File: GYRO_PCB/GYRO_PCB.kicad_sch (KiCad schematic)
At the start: 17 parts, among them J1 Pmod GYRO, J2 FLASH Socket 1, J3 FLASH Socket 2, J4 Power Terminal, J5 Battery Switch, U1 NUCLEO64-F446RE

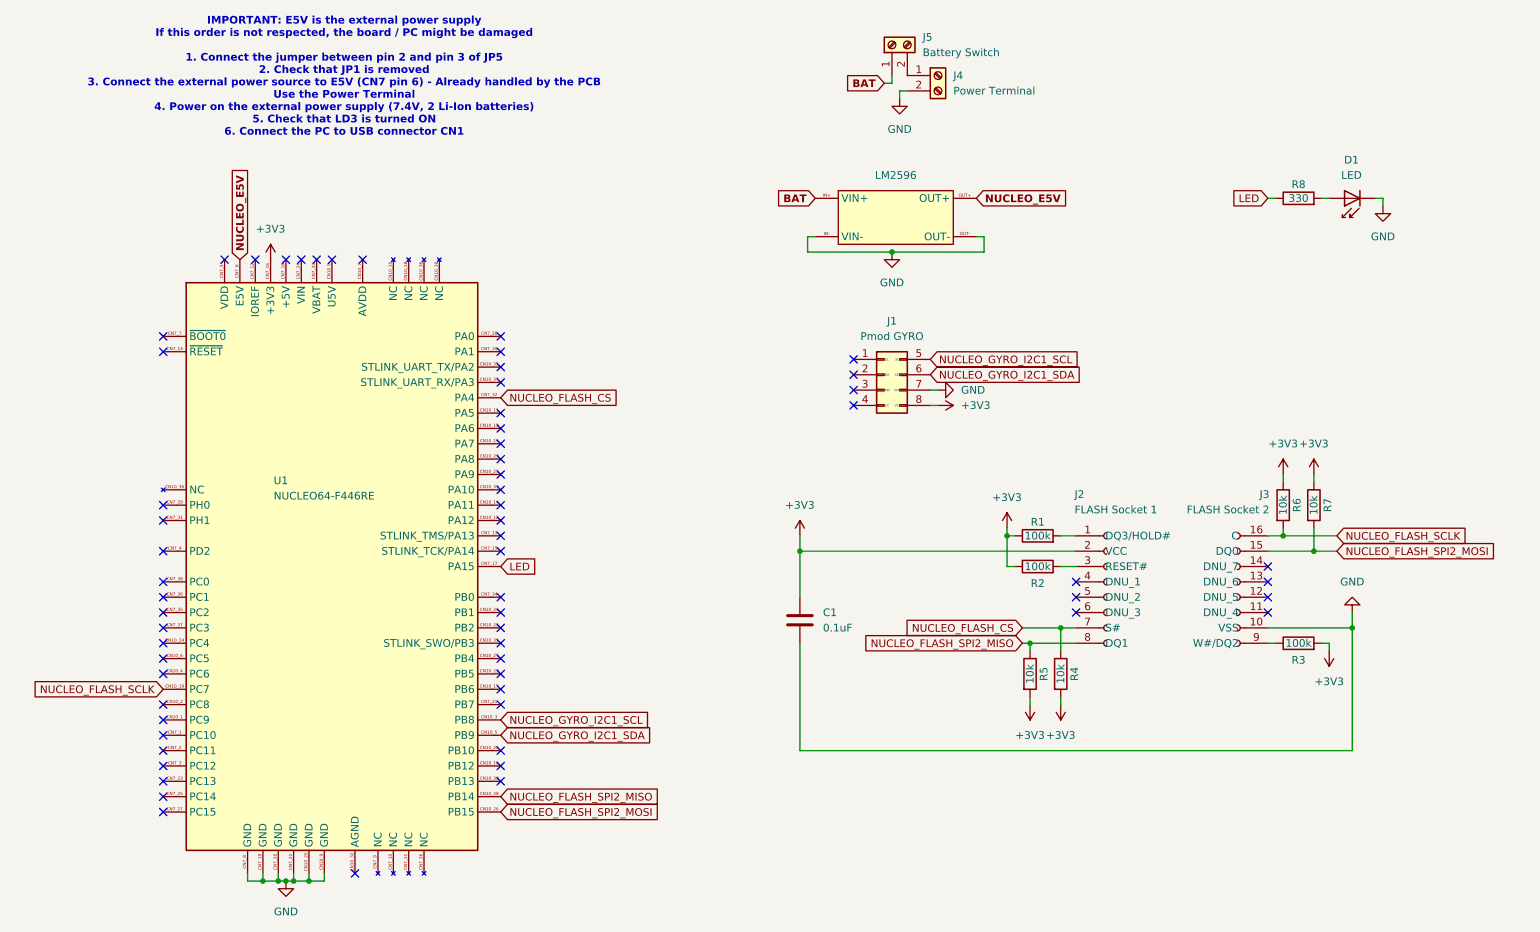
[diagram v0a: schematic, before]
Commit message: feat: add push button
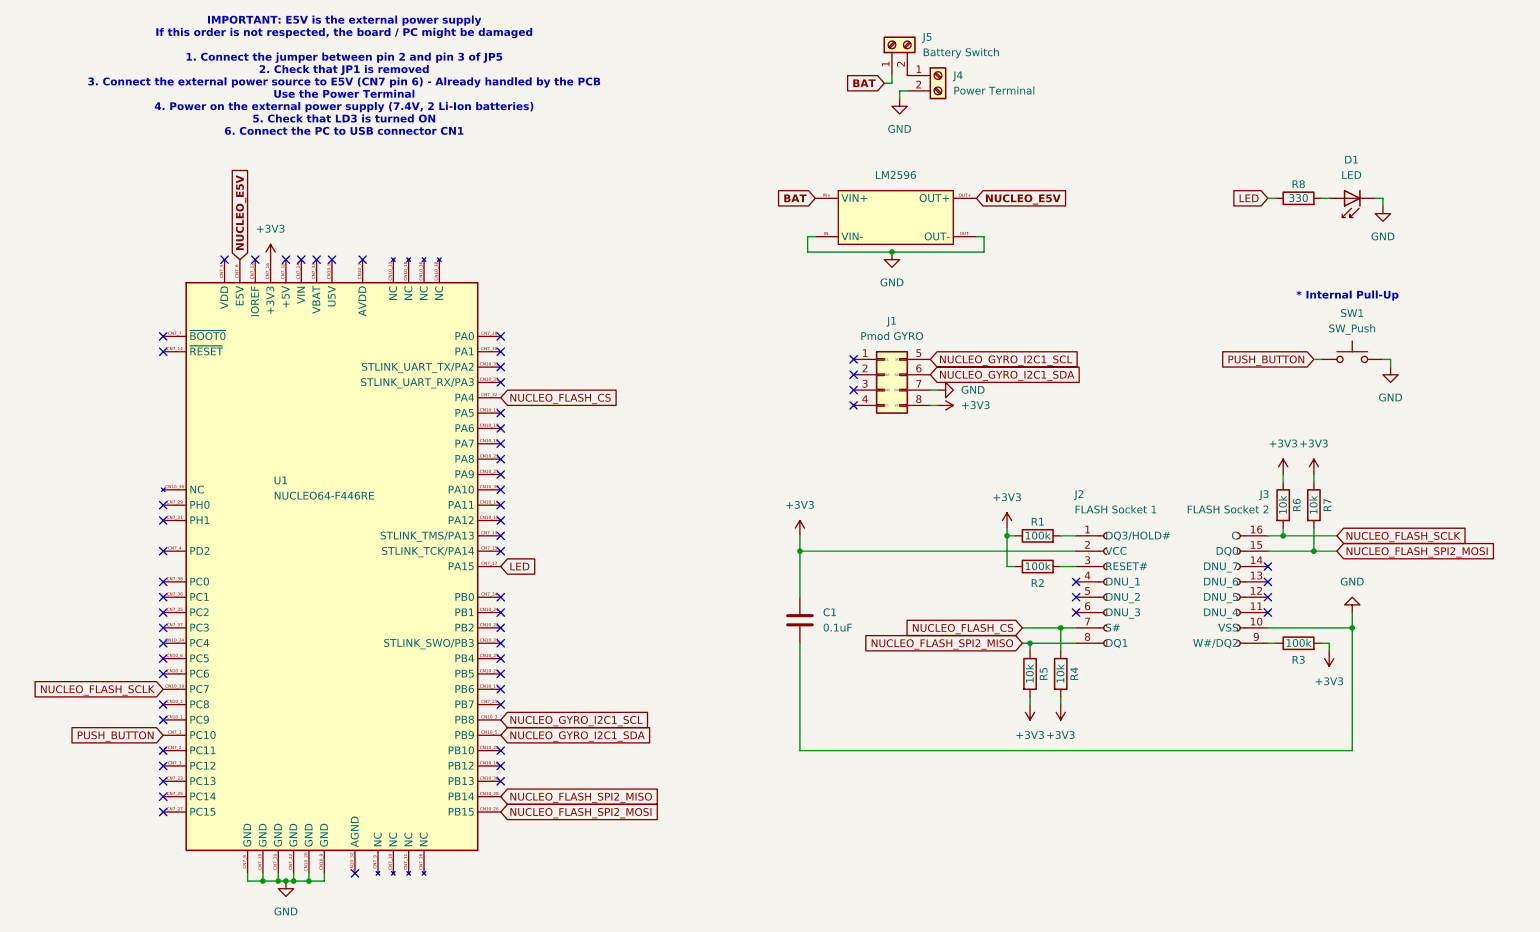
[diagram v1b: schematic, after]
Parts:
- added SW1: SW_Push, Connector_PinSocket_2.54mm:PinSocket_1x02_P2.54mm_Vertical, symbol Switch:SW_Push
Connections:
- net GND: now also SW1.2
- net PUSH_BUTTON: now reaches U1.CN7_1 (PC10)
- net PUSH_BUTTON: now also SW1.1
- no-connect marks 64 -> 63
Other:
- note added: "* Internal Pull-Up"
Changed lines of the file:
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@@
 				(thickness 0.254)
 				(bold yes)
+				(color 255 0 0 1)
+			)
+		)
+	)
+	(text "* Internal Pull-Up"
+		(exclude_from_sim no)
+		(at 248.158 74.676 0)
+		(effects
+			(font
+				(size 1.27 1.27)
+				(thickness 0.254)
+				(bold yes)
+				(color 255 0 0 1)
 			)
 		)
@@
 	)
 	(no_connect
-		(at 52.07 147.32)
-	)
-	(no_connect
 		(at 234.95 124.46)
 	)
@@
 	(wire
 		(pts
+			(xy 255.27 86.36) (xy 255.27 85.09)
+		)
+		(stroke
+			(width 0)
+			(type default)
+		)
+	)
+	(wire
+		(pts
 			(xy 254 58.42) (xy 252.73 58.42)
 		)
@@
 	(wire
 		(pts
+			(xy 254 85.09) (xy 255.27 85.09)
+		)
+		(stroke
+			(width 0)
+			(type default)
+		)
+	)
+	(wire
+		(pts
 			(xy 248.92 149.86) (xy 248.92 129.54)
 		)
@@
 	(wire
 		(pts
+			(xy 242.57 85.09) (xy 243.84 85.09)
+		)
+		(stroke
+			(width 0)
+			(type default)
+		)
+	)
+	(wire
+		(pts
 			(xy 234.95 132.08) (xy 236.22 132.08)
 		)
@@
 		)
 	)
+	(global_label "PUSH_BUTTON"
+		(shape input)
+		(at 242.57 85.09 180)
+		(fields_autoplaced yes)
+		(effects
+			(font
+				(size 1.27 1.27)
+			)
+			(justify right)
+		)
+		(property "Intersheetrefs" "${INTERSHEET_REFS}"
+			(at 226.28 85.09 0)
+			(effects
+				(font
+					(size 1.27 1.27)
+				)
+				(justify right)
+				(hide yes)
+			)
+		)
+	)
 	(global_label "NUCLEO_GYRO_I2C1_SCL"
 		(shape input)
@@
 		)
 	)
+	(global_label "PUSH_BUTTON"
+		(shape input)
+		(at 52.07 147.32 180)
+		(fields_autoplaced yes)
+		(effects
+			(font
+				(size 1.27 1.27)
+			)
+			(justify right)
+		)
+		(property "Intersheetrefs" "${INTERSHEET_REFS}"
+			(at 35.78 147.32 0)
+			(effects
+				(font
+					(size 1.27 1.27)
+				)
+				(justify right)
+				(hide yes)
+			)
+		)
+	)
 	(global_label "NUCLEO_FLASH_SPI2_MOSI"
 		(shape input)
@@
 	)
 	(symbol
+		(lib_id "Switch:SW_Push")
+		(at 248.92 85.09 0)
+		(unit 1)
+		(exclude_from_sim no)
+		(in_bom yes)
+		(on_board yes)
+		(dnp no)
+		(fields_autoplaced yes)
+		(property "Reference" "SW1"
+			(at 248.92 77.47 0)
+			(effects
+				(font
+					(size 1.27 1.27)
+				)
+			)
+		)
+		(property "Value" "SW_Push"
+			(at 248.92 80.01 0)
+			(effects
+				(font
+					(size 1.27 1.27)
+				)
+			)
+		)
+		(property "Footprint" "Connector_PinSocket_2.54mm:PinSocket_1x02_P2.54mm_Vertical"
+			(at 248.92 80.01 0)
+			(effects
+				(font
+					(size 1.27 1.27)
+				)
+				(hide yes)
+			)
+		)
+		(property "Datasheet" "~"
+			(at 248.92 80.01 0)
+			(effects
+				(font
+					(size 1.27 1.27)
+				)
+				(hide yes)
+			)
+		)
+		(property "Description" "Push button switch, generic, two pins"
+			(at 248.92 85.09 0)
+			(effects
+				(font
+					(size 1.27 1.27)
+				)
+				(hide yes)
+			)
+		)
+		(pin "2"
+		)
+		(pin "1"
+		)
+		(instances
+			(project ""
+				(path "/0bddacac-ad2f-4aa4-b051-0a05ac7aff99"
+					(reference "SW1")
+					(unit 1)
+				)
+			)
+		)
+	)
+	(symbol
 		(lib_id "power:+3V3")
 		(at 191.77 113.03 0)
@@
 					(unit 1)
 				)
+			)
+		)
+	)
+	(symbol
+		(lib_id "power:GND")
+		(at 255.27 86.36 0)
+		(unit 1)
+		(exclude_from_sim no)
+		(in_bom yes)
+		(on_board yes)
+		(dnp no)
+		(fields_autoplaced yes)
+		(property "Reference" "#PWR016"
+			(at 255.27 92.71 0)
+			(effects
+				(font
+					(size 1.27 1.27)
+				)
+				(hide yes)
+			)
+		)
+		(property "Value" "GND"
+			(at 255.27 91.44 0)
+			(effects
+				(font
+					(size 1.27 1.27)
+				)
+			)
+		)
+		(property "Footprint" ""
+			(at 255.27 86.36 0)
+			(effects
+				(font
+					(size 1.27 1.27)
+				)
+				(hide yes)
+			)
+		)
+		(property "Datasheet" ""
+			(at 255.27 86.36 0)
+			(effects
+				(font
+					(size 1.27 1.27)
+				)
+				(hide yes)
+			)
+		)
+		(property "Description" "Power symbol creates a global label with name \"GND\" , ground"
+			(at 255.27 86.36 0)
+			(effects
+				(font
+					(size 1.27 1.27)
+				)
+				(hide yes)
+			)
+		)
+		(pin "1"
+		)
+		(instances
+			(project ""
+				(path "/0bddacac-ad2f-4aa4-b051-0a05ac7aff99"
+					(reference "#PWR016")
+					(unit 1)
+				)
